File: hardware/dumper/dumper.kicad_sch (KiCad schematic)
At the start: 15 parts, among them J1 /Reset, J2 Clock In, J5 2816 /WR disconnect, J8 arduino 5, J9 arduino 7, SW1 SW_MEC_5E, U2 DS1225Y, U3 74HCT373, U4 PIC70xx/TMS70xx

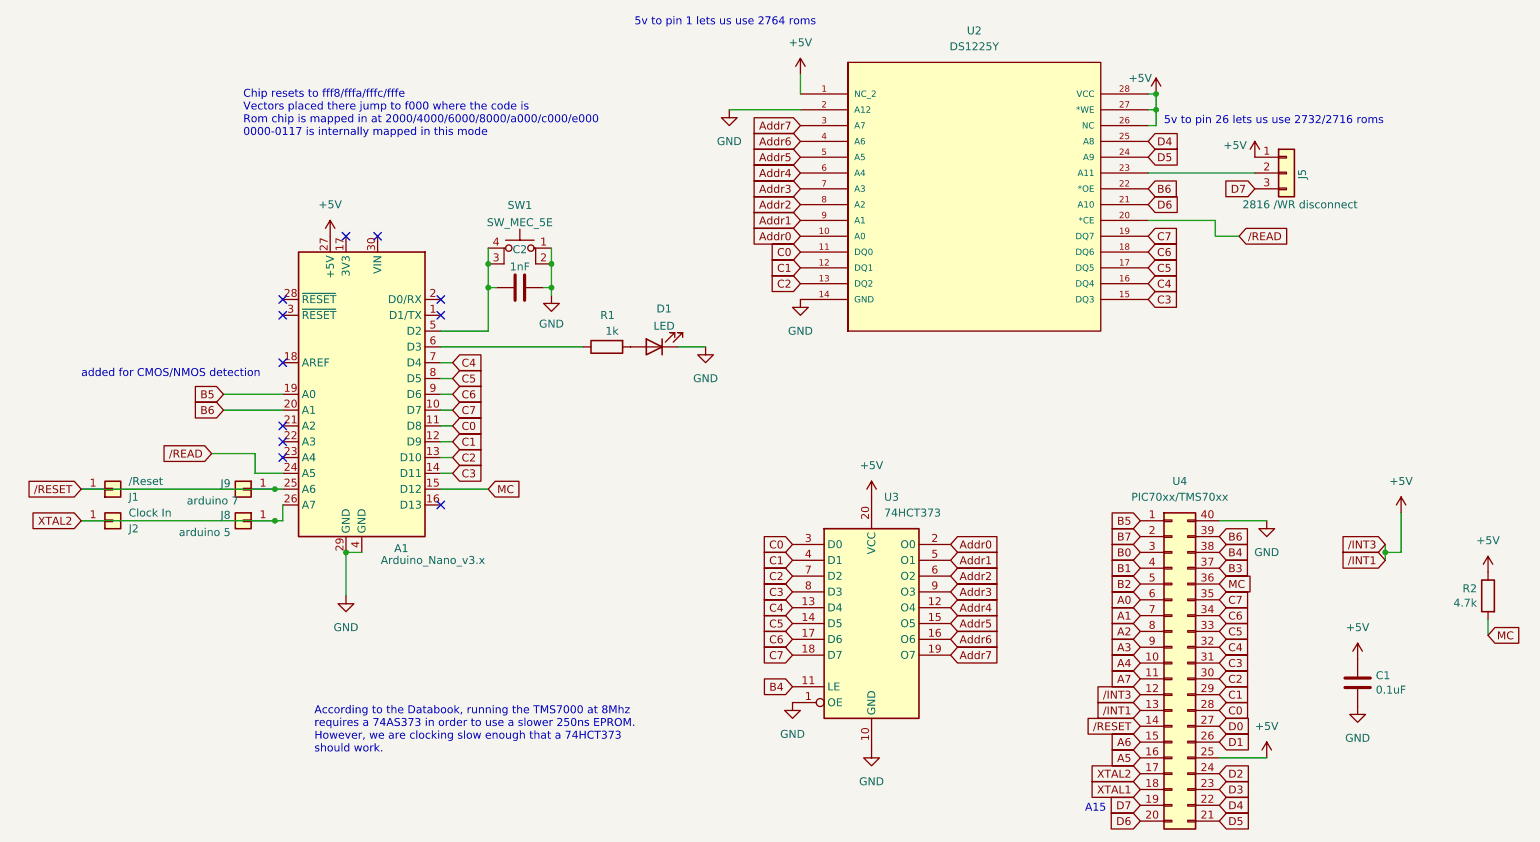
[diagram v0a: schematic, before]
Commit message: Updates for memory-mapped IO
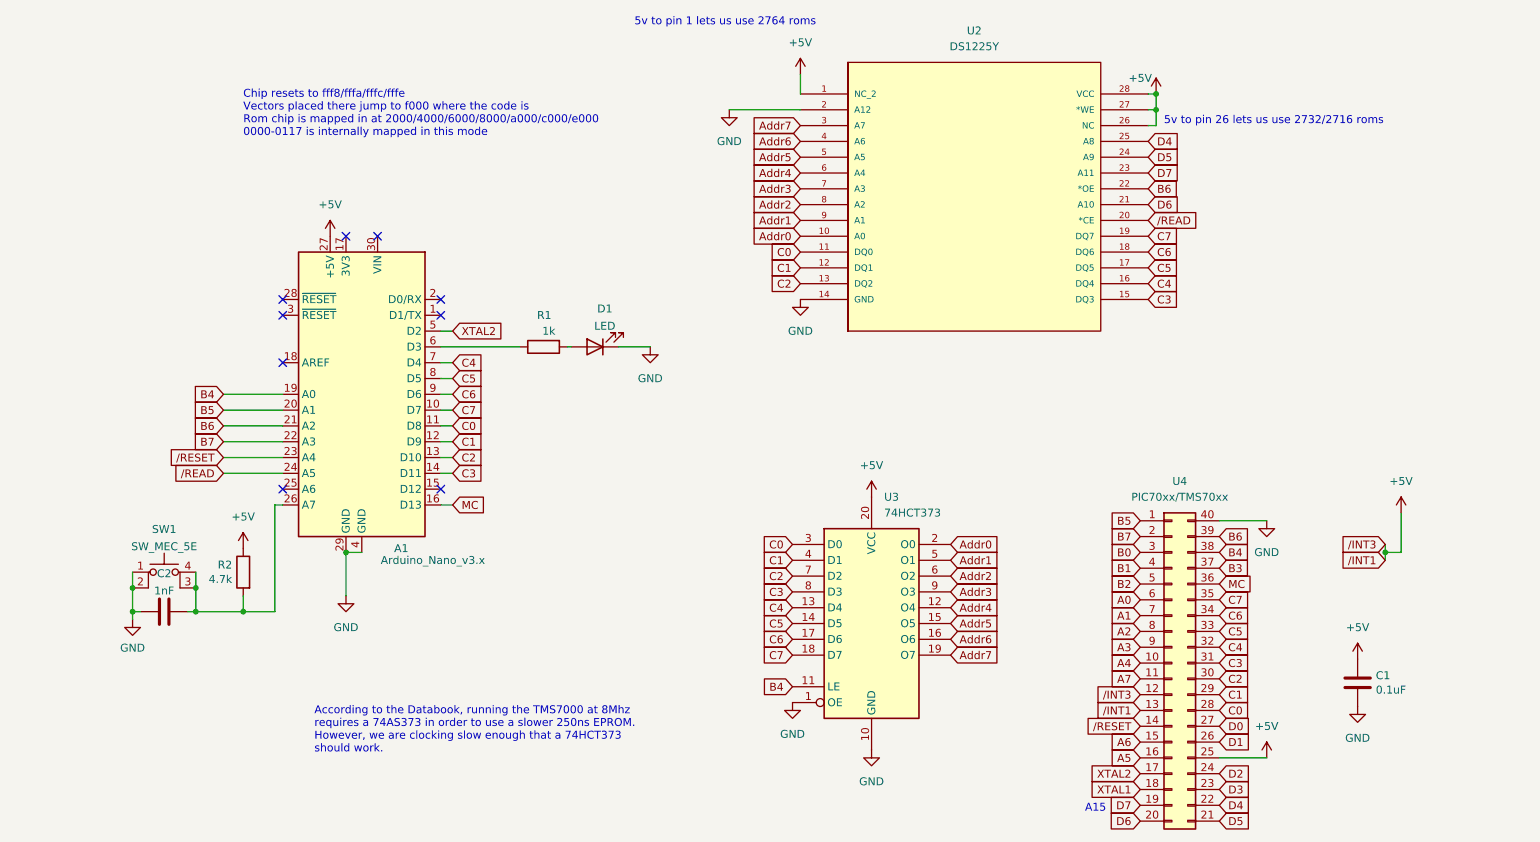
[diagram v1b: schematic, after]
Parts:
- removed J1: /Reset, Connector_PinHeader_2.54mm:PinHeader_1x01_P2.54mm_Vertical, symbol Connector_Generic:Conn_01x01
- removed J2: Clock In, Connector_PinHeader_2.54mm:PinHeader_1x01_P2.54mm_Vertical, symbol Connector_Generic:Conn_01x01
- removed J5: 2816 /WR disconnect, Connector_PinHeader_2.54mm:PinHeader_1x03_P2.54mm_Vertical, symbol Connector_Generic:Conn_01x03
- removed J8: arduino 5, Connector_PinHeader_2.54mm:PinHeader_1x01_P2.54mm_Vertical, symbol Connector_Generic:Conn_01x01
- removed J9: arduino 7, Connector_PinHeader_2.54mm:PinHeader_1x01_P2.54mm_Vertical, symbol Connector_Generic:Conn_01x01
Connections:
- net B4: now also A1.19 (A0)
- net B5: now also A1.20 (A1); no longer A1.19 (A0)
- net B6: now also A1.21 (A2); no longer A1.20 (A1)
- net B7: now also A1.22 (A3)
- net D7: now also U2.23 (A11)
- net MC: now also A1.16 (D13); no longer A1.15 (D12), R2.2
- net XTAL2: now also A1.5 (D2); no longer A1.26 (A7)
- net /RESET: now also A1.23 (A4); no longer A1.25 (A6)
- net at C2.2, SW1.3 (K), SW1.4 (A): now also A1.26 (A7), R2.2; no longer A1.5 (D2)
- no-connect marks 11 -> 9
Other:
- note removed: "added for CMOS/NMOS detection"
- moved on the sheet: C2, D1, R1, SW1

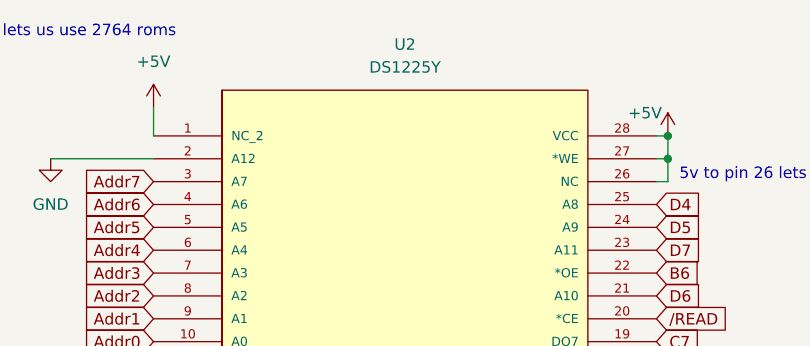
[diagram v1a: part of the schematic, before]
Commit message: laid out rev b dumper
juggled all the address lines and additional arduino wiring to facilitate parallel reads and CT dumping
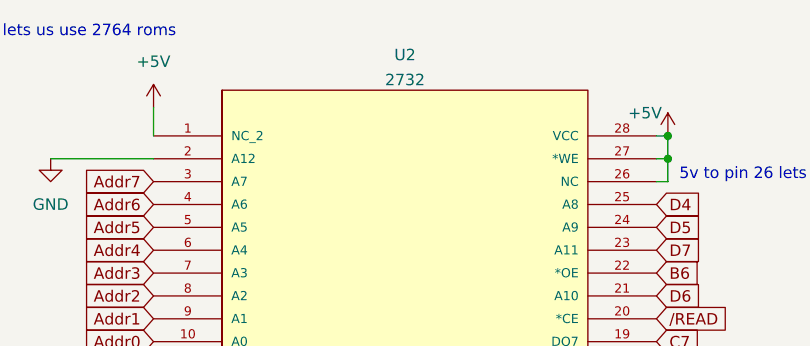
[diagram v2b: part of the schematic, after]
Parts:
- U2: value DS1225Y -> 2732
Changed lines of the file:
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@@
   (symbol (lib_id "Frank Misc:DS1225Y-150") (at 139.7 39.37 0) (unit 1)
     (in_bom yes) (on_board yes) (fields_autoplaced)
-    (property "Reference" "U2" (id 0) (at 167.64 29.21 0))
-    (property "Value" "DS1225Y" (id 1) (at 167.64 31.75 0))
+    (property "Reference" "U2" (id 0) (at 167.64 30.3743 0))
+    (property "Value" "2732" (id 1) (at 167.64 33.1494 0))
     (property "Footprint" "Evan's misc parts:21-0245A_28" (id 2) (at 139.7 39.37 0)
       (effects (font (size 1.27 1.27)) (justify left bottom) hide)
@@
     )
     (path "/5bab83de-2cb2-4fe3-8877-7d62e5b0d55c"
-      (reference "U2") (unit 1) (value "DS1225Y") (footprint "Evan's misc parts:21-0245A_28")
+      (reference "U2") (unit 1) (value "2732") (footprint "Evan's misc parts:21-0245A_28")
     )
     (path "/30e22497-a1d6-4c33-93b9-15b0695925a2"
